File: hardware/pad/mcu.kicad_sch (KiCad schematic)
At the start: 2 parts, among them J4 SWD

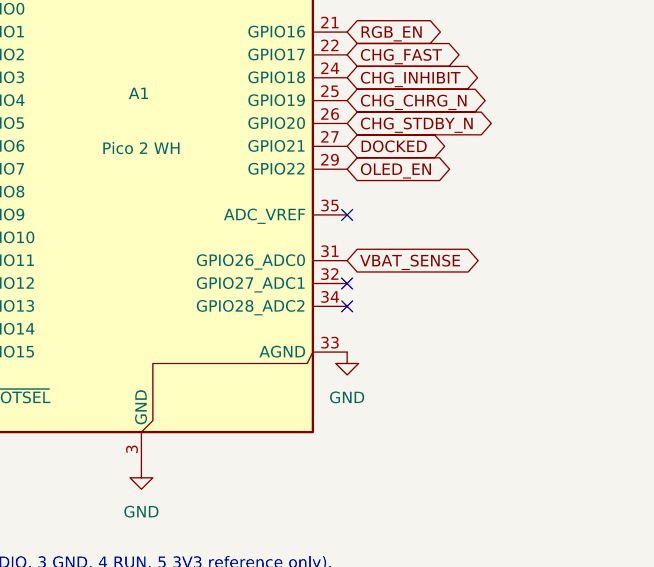
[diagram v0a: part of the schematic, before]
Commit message: Pad: display on 9-pin JST-PH with backlight MOSFET (GP27), pogo cable connector; pogo board schematic; guide updated to final refs
Co-Authored-By: Claude Opus 5.5 <noreply@anthropic.com>
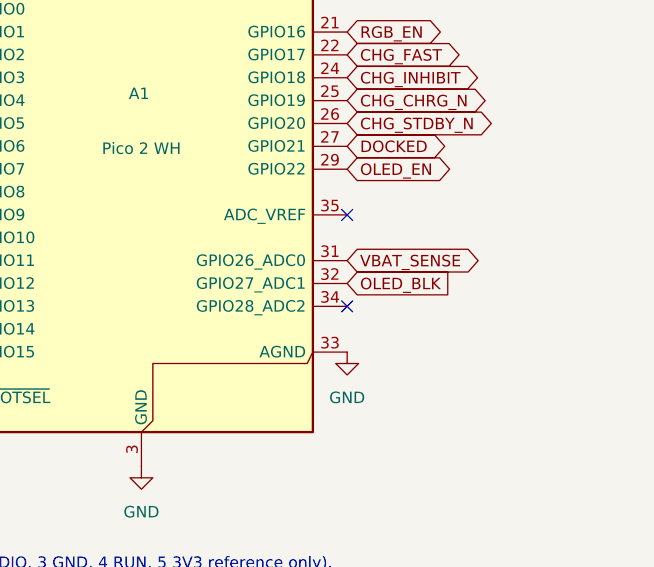
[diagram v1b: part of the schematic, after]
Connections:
- net OLED_BLK: now reaches A1.32 (GPIO27_ADC1)
- no-connect marks 12 -> 11
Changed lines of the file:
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@@
-	)
-	(no_connect
-		(at 142.24 114.3)
 	)
 	(no_connect
@@
 			)
 		)
+	)
+	(global_label "OLED_BLK"
+		(shape input)
+		(at 142.24 114.3 0)
+		(fields_autoplaced yes)
+		(effects
+			(font
+				(size 1.27 1.27)
+			)
+			(justify left)
+		)
+		(property "Intersheetrefs" "${INTERSHEET_REFS}"
+			(at 154.5385 114.3 0)
+			(hide yes)
+			(show_name no)
+			(do_not_autoplace no)
+			(effects
+				(font
+					(size 1.27 1.27)
+				)
+				(justify left)
+			)
+		)

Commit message: Pad PCB: first placement; SWD header removed, side-entry JST connectors, new footprints
- J4 (SWD) removed; A1 on the NoSWD Pico socket footprint (holes would sit under key 5)
- J1/J7/J2/J3 side-entry JST (S*B), J5 stays vertical
- New footprints: PEC11R encoder (13.2 mm lugs), SOIC-8-1EP hand-solder (TP4056),
  narrower SOT-563 pads
- All footprints placed on the 100 x 92 board; ring LEDs radial at R 12.7,
  encoders at 16.6 / 83.4; edge clearance rule 0.2 mm
- PCB_PLACEMENT.md and placement drawings in docs/

Co-Authored-By: Claude Opus 5.5 <noreply@anthropic.com>
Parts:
- removed J4: SWD, Connector_PinHeader_2.54mm:PinHeader_1x05_P2.54mm_Vertical, symbol Connector:Conn_01x05_Pin
- A1: footprint dock:RaspberryPi_Pico2W_Socket -> dock:RaspberryPi_Pico2W_Socket_NoSWD
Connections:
- no-connect marks 11 -> 14
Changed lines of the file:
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@@
 		(at 96.52 127)
-	)
-	(wire
-		(pts
-			(xy 81.28 76.2) (xy 96.52 76.2)
-		)
-		(stroke
-			(width 0)
-			(type default)
-		)
-	)
-	(wire
-		(pts
-			(xy 81.28 68.58) (xy 96.52 68.58)
-		)
-		(stroke
-			(width 0)
-			(type default)
-		)
-	)
-	(wire
-		(pts
-			(xy 81.28 71.12) (xy 96.52 71.12)
-		)
-		(stroke
-			(width 0)
-			(type default)
-		)
 	)
 	(global_label "OLED_CS"
@@
 		(property "Intersheetrefs" "${INTERSHEET_REFS}"
 			(at 96.52 106.68 0)
-			(hide yes)
-			(show_name no)
-			(do_not_autoplace no)
-			(effects
-				(font
-					(size 1.27 1.27)
-				)
-			)
-		)
-	)
-	(global_label "+3V3"
-		(shape bidirectional)
-		(at 81.28 78.74 0)
-		(fields_autoplaced yes)
-		(effects
-			(font
-				(size 1.27 1.27)
-			)
-			(justify left)
-		)
-		(property "Intersheetrefs" "${INTERSHEET_REFS}"
-			(at 81.28 78.74 0)
 			(hide yes)
 			(show_name no)
@@
 			)
 		)
-		(property "Footprint" "dock:RaspberryPi_Pico2W_Socket"
+		(property "Footprint" "dock:RaspberryPi_Pico2W_Socket_NoSWD"
 			(at 119.38 99.06 0)
 			(hide yes)
@@
 	(symbol
 		(lib_id "power:GND")
-		(at 81.28 73.66 90)
-		(unit 1)
-		(body_style 1)
-		(exclude_from_sim no)
-		(in_bom yes)
-		(on_board yes)
-		(in_pos_files yes)
-		(dnp no)
-		(fields_autoplaced yes)
-		(property "Reference" "#PWR019"
-			(at 87.63 73.66 0)
-			(hide yes)
-			(show_name no)
-			(do_not_autoplace no)
-			(effects
-				(font
-					(size 1.27 1.27)
-				)
-			)
-		)
-		(property "Value" "GND"
-			(at 85.09 73.6599 90)
-			(show_name no)
-			(do_not_autoplace no)
-			(effects
-				(font
-					(size 1.27 1.27)
-				)
-				(justify right)
-			)
-		)
-		(property "Footprint" ""
-			(at 81.28 73.66 0)
-			(hide yes)
-			(show_name no)
-			(do_not_autoplace no)
-			(effects
-				(font
-					(size 1.27 1.27)
-				)
-			)
-		)
-		(property "Datasheet" ""
-			(at 81.28 73.66 0)
-			(hide yes)
-			(show_name no)
-			(do_not_autoplace no)
-			(effects
-				(font
-					(size 1.27 1.27)
-				)
-			)
-		)
-		(property "Description" "Power symbol creates a global label with name \"GND\" , ground"
-			(at 81.28 73.66 0)
-			(hide yes)
-			(show_name no)
-			(do_not_autoplace no)
-			(effects
-				(font
-					(size 1.27 1.27)
-				)
-			)
-		)
-		(pin "1"
-		)
-		(instances
-			(project "pad"
-				(path "/e7f715eb-7c18-4c70-befb-dbed60a95ef2/f913b2b7-06cc-4745-bf8c-45e5b76c74d5"
-					(reference "#PWR019")
-					(unit 1)
-				)
-			)
-		)
-	)
-	(symbol
-		(lib_id "Connector:Conn_01x05_Pin")
-		(at 76.2 73.66 0)
-		(unit 1)
-		(body_style 1)
-		(exclude_from_sim no)
-		(in_bom yes)
-		(on_board yes)
-		(in_pos_files yes)
-		(dnp no)
-		(property "Reference" "J4"
-			(at 76.2 64.77 0)
-			(show_name no)
-			(do_not_autoplace no)
-			(effects
-				(font
-					(size 1.27 1.27)
-				)
-			)
-		)
-		(property "Value" "SWD"
-			(at 76.2 82.55 0)
-			(show_name no)
-			(do_not_autoplace no)
-			(effects
-				(font
-					(size 1.27 1.27)
-				)
-			)
-		)
-		(property "Footprint" "Connector_PinHeader_2.54mm:PinHeader_1x05_P2.54mm_Vertical"
-			(at 76.2 73.66 0)
-			(hide yes)
-			(show_name no)
-			(do_not_autoplace no)
-			(effects
-				(font
-					(size 1.27 1.27)
-				)
-			)
-		)
-		(property "Datasheet" ""
-			(at 76.2 73.66 0)
-			(hide yes)
-			(show_name no)
-			(do_not_autoplace no)
-			(effects
-				(font
-					(size 1.27 1.27)
-				)
-			)
-		)
-		(property "Description" "Generic connector, single row, 01x05, script generated"
-			(at 76.2 73.66 0)
-			(hide yes)
-			(show_name no)
-			(do_not_autoplace no)
-			(effects
-				(font
-					(size 1.27 1.27)
-				)
-			)
-		)
-		(pin "1"
-		)
-		(pin "2"
-		)
-		(pin "3"
-		)
-		(pin "4"
-		)
-		(pin "5"
-		)
-		(instances
-			(project "pad"
-				(path "/e7f715eb-7c18-4c70-befb-dbed60a95ef2/f913b2b7-06cc-4745-bf8c-45e5b76c74d5"
-					(reference "J4")
-					(unit 1)
-				)
-			)
-		)
-	)
-	(symbol
-		(lib_id "power:GND")
 		(at 119.38 134.62 0)
 		(unit 1)
@@
 		)
 	)
+	(no_connect
+		(at 96.52 68.58)
+	)
+	(no_connect
+		(at 96.52 71.12)
+	)
+	(no_connect
+		(at 96.52 76.2)
+	)
 )
